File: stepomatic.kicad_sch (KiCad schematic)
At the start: 30 parts, among them J1 I2C, J2 Conn_01x05, J4 USB_B_Micro, Q1 MMBT3904, Q2 MMBT3904, SW1 Mode, SW2 RST, U1 HDC1080DMBR, U2 AMS1117-3.3, U3 ULN2003A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

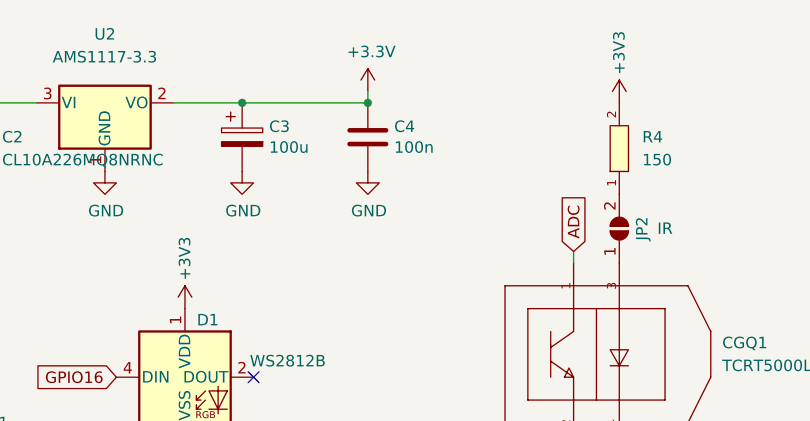
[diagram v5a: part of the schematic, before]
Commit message: Fix wrong capacitor
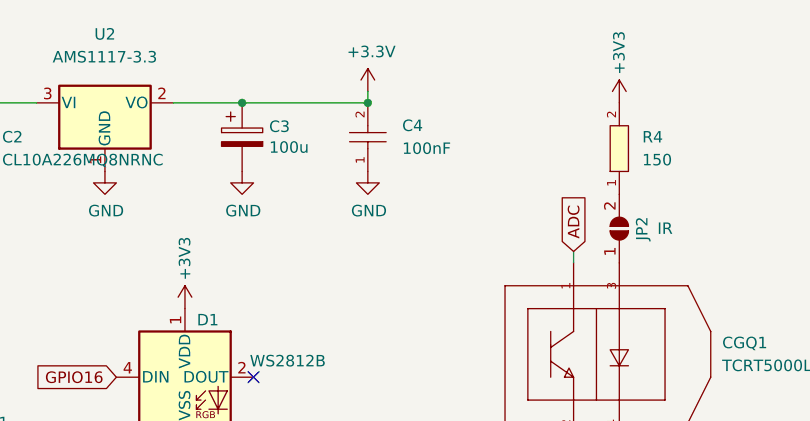
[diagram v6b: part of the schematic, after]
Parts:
- removed C4: 100n, Capacitor_SMD:C_0805_2012Metric, symbol Device:C
- added C4: 100nF, footprint:C0402, symbol CL05B104KO5NNNC:CL05B104KO5NNNC
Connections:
- net +3V3: now also C4.2
- net GND: now also C4.1
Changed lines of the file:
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@@
     (company "Besmer Labs")
   )
+  (junction (at 207.01 39.37) (diameter 0) (color 0 0 0 0)
+  )
   (junction (at 193.04 39.37) (diameter 0) (color 0 0 0 0)
-  )
-  (junction (at 207.01 39.37) (diameter 0) (color 0 0 0 0)
   )
   (junction (at 88.9 81.28) (diameter 0) (color 0 0 0 0)
@@
     (pin "4")
   )
+  (symbol (lib_id "CL05B104KO5NNNC:CL05B104KO5NNNC") (at 207.01 43.18 90) (unit 1)
+    (in_bom yes) (on_board yes) (fields_autoplaced)
+    (property "Reference" "C4" (id 0) (at 210.82 41.9099 90)
+      (effects (font (size 1.27 1.27)) (justify right))
+    )
+    (property "Value" "100nF" (id 1) (at 210.82 44.4499 90)
+      (effects (font (size 1.27 1.27)) (justify right))
+    )
+    (property "Footprint" "footprint:C0402" (id 2) (at 217.17 43.18 0)
+      (effects (font (size 1.27 1.27) italic) hide)
+    )
+    (property "Datasheet" "https://item.szlcsc.com/15869.html" (id 3) (at 206.883 45.466 0)
+      (effects (font (size 1.27 1.27)) (justify left) hide)
+    )
+    (property "LCSC" "C1525" (id 4) (at 207.01 43.18 0)
+      (effects (font (size 1.27 1.27)) hide)
+    )
+    (property "JLC" "" (id 5) (at 207.01 43.18 0)
+      (effects (font (size 1.27 1.27)) hide)
+    )
+    (pin "1")
+    (pin "2")
+  )
   (symbol (lib_id "Mechanical:MountingHole") (at 125.73 142.24 0) (unit 1)
     (in_bom no) (on_board yes) (fields_autoplaced)
@@
     )
     (pin "1")
-  )
-  (symbol (lib_id "Device:C") (at 207.01 43.18 0) (unit 1)
-    (in_bom yes) (on_board yes)
-    (property "Reference" "C4" (id 0) (at 209.931 42.0116 0)
-      (effects (font (size 1.27 1.27)) (justify left))
-    )
-    (property "Value" "100n" (id 1) (at 209.931 44.323 0)
-      (effects (font (size 1.27 1.27)) (justify left))
-    )
-    (property "Footprint" "Capacitor_SMD:C_0805_2012Metric" (id 2) (at 207.9752 46.99 0)
-      (effects (font (size 1.27 1.27)) hide)
-    )
-    (property "Datasheet" "~" (id 3) (at 207.01 43.18 0)
-      (effects (font (size 1.27 1.27)) hide)
-    )
-    (property "JLC" "" (id 5) (at 207.01 43.18 0)
-      (effects (font (size 1.27 1.27)) hide)
-    )
-    (property "LCSC" "C15008" (id 6) (at 209.931 42.0116 0)
-      (effects (font (size 1.27 1.27)) hide)
-    )
-    (pin "1")
-    (pin "2")
   )
   (symbol (lib_id "Mechanical:MountingHole") (at 125.095 161.29 0) (unit 1)
@@
       (reference "C3") (unit 1) (value "100u") (footprint "footprint:CASE-B_3528")
     )
-    (path "/997e98a3-7fb1-4b0a-aef3-53f70b9f03e9"
-      (reference "C4") (unit 1) (value "100n") (footprint "Capacitor_SMD:C_0805_2012Metric")
+    (path "/060122c0-b2a7-48a4-b1fe-01044e6f558d"
+      (reference "C4") (unit 1) (value "100nF") (footprint "footprint:C0402")
     )
     (path "/5bb5ca00-b4de-4288-b93f-8dde24e62e4c"

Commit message: Remove JLC property
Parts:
- J2: JLC_URL https://jlcpcb.com/partdetail/Jst-B5B_EH_LF_SN/C157991 -> (none)
- SW1, SW2: JLC_URL https://jlcpcb.com/partdetail/XkbConnectivity-TS_1187A_B_AB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 -> (none)
- U2: JLC_URL https://jlcpcb.com/partdetail/Advanced_MonolithicSystems-AM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 -> (none)
- U3: JLC_URL https://jlcpcb.com/partdetail/TexasInstruments-ULN2003ADR/C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 -> (none)
- U4: JLC_URL https://jlcpcb.com/partdetail/wch_jiangsu_Qin_heng-CH340C/C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 -> (none)
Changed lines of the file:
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@@
-      (effects (font (size 1.27 1.27)) hide)
-    )
-    (property "JLC" "" (id 5) (at 207.01 43.18 0)
       (effects (font (size 1.27 1.27)) hide)
     )
@@
       (effects (font (size 1.27 1.27)) hide)
     )
-    (property "JLC" "" (id 4) (at 125.73 142.24 0)
-      (effects (font (size 1.27 1.27)) hide)
-    )
     (property "LCSC" "DNP" (id 5) (at 125.73 142.24 0)
       (effects (font (size 1.27 1.27)) hide)
@@
       (effects (font (size 1.27 1.27)) hide)
     )
-    (property "JLC" "" (id 4) (at 125.73 154.94 0)
-      (effects (font (size 1.27 1.27)) hide)
-    )
     (property "LCSC" "DNP" (id 5) (at 125.73 154.94 0)
       (effects (font (size 1.27 1.27)) hide)
@@
     )
     (property "Datasheet" "~" (id 3) (at 193.04 43.18 0)
-      (effects (font (size 1.27 1.27)) hide)
-    )
-    (property "JLC" "" (id 5) (at 193.04 43.18 0)
       (effects (font (size 1.27 1.27)) hide)
     )
@@
       (effects (font (size 1.27 1.27)) (justify left top) hide)
     )
-    (property "JLC" "" (id 4) (at 186.69 69.85 0)
-      (effects (font (size 1.27 1.27)) hide)
-    )
     (property "LCSC" "DNP" (id 5) (at 186.69 69.85 0)
       (effects (font (size 1.27 1.27)) hide)
@@
       (effects (font (size 1.27 1.27)) (justify left) hide)
     )
-    (property "JLC" "" (id 5) (at 46.99 135.89 0)
-      (effects (font (size 1.27 1.27)) hide)
-    )
     (property "LCSC" "C20526" (id 6) (at 41.91 134.6199 0)
       (effects (font (size 1.27 1.27)) hide)
@@
     )
     (property "LCSC" "C1525" (id 4) (at 83.82 66.04 0)
-      (effects (font (size 1.27 1.27)) hide)
-    )
-    (property "JLC" "" (id 5) (at 83.82 66.04 0)
       (effects (font (size 1.27 1.27)) hide)
     )
@@
       (effects (font (size 1.27 1.27)) hide)
     )
-    (property "JLC" "" (id 4) (at 234.95 53.34 0)
-      (effects (font (size 1.27 1.27)) hide)
-    )
     (property "LCSC" "DNP" (id 5) (at 234.95 53.34 0)
       (effects (font (size 1.27 1.27)) hide)
@@
       (effects (font (size 1.27 1.27)) hide)
     )
-    (property "JLC" "" (id 5) (at 95.25 66.04 0)
-      (effects (font (size 1.27 1.27)) hide)
-    )
     (pin "1")
     (pin "2")
@@
     )
     (property "LCSC" "C22961" (id 4) (at 121.92 86.36 0)
-      (effects (font (size 1.27 1.27)) hide)
-    )
-    (property "JLC" "" (id 5) (at 121.92 86.36 0)
       (effects (font (size 1.27 1.27)) hide)
     )
@@
       (effects (font (size 1.27 1.27)) hide)
     )
-    (property "JLC_URL" "https://jlcpcb.com/partdetail/Advanced_MonolithicSystems-AMS1117_33/C6186" (id 5) (at 177.8 39.37 0)
-      (effects (font (size 1.27 1.27)) hide)
-    )
-    (property "JLC" "" (id 6) (at 177.8 39.37 0)
-      (effects (font (size 1.27 1.27)) hide)
-    )
     (property "LCSC" "C6186" (id 7) (at 177.8 31.75 0)
       (effects (font (size 1.27 1.27)) hide)
@@
       (effects (font (size 1.27 1.27)) hide)
     )
-    (property "JLC" "" (id 5) (at 55.88 149.86 0)
-      (effects (font (size 1.27 1.27)) hide)
-    )
     (property "LCSC" "C25752" (id 6) (at 55.88 146.05 0)
       (effects (font (size 1.27 1.27)) hide)
@@
     )
     (property "LCSC" "C59461" (id 4) (at 162.56 44.45 0)
-      (effects (font (size 1.27 1.27)) hide)
-    )
-    (property "JLC" "" (id 5) (at 162.56 44.45 0)
       (effects (font (size 1.27 1.27)) hide)
     )
@@
       (effects (font (size 1.27 1.27)) hide)
     )
-    (property "JLC" "" (id 4) (at 125.095 161.29 0)
-      (effects (font (size 1.27 1.27)) hide)
-    )
     (property "LCSC" "DNP" (id 5) (at 125.095 161.29 0)
       (effects (font (size 1.27 1.27)) hide)
@@
     )
     (property "Datasheet" "~" (id 3) (at 125.73 148.59 0)
-      (effects (font (size 1.27 1.27)) hide)
-    )
-    (property "JLC" "" (id 4) (at 125.73 148.59 0)
       (effects (font (size 1.27 1.27)) hide)
     )
@@
     )
     (property "Datasheet" "http://www.ti.com/lit/ds/symlink/uln2003a.pdf" (id 3) (at 204.47 125.73 0)
-      (effects (font (size 1.27 1.27)) hide)
-    )
-    (property "JLC_URL" "https://jlcpcb.com/partdetail/TexasInstruments-ULN2003ADR/C7512" (id 5) (at 201.93 120.65 0)
-      (effects (font (size 1.27 1.27)) hide)
-    )
-    (property "JLC" "" (id 6) (at 201.93 120.65 0)
       (effects (font (size 1.27 1.27)) hide)
     )
@@
       (effects (font (size 1.27 1.27)) hide)
     )
-    (property "JLC" "" (id 5) (at 55.88 135.89 0)
-      (effects (font (size 1.27 1.27)) hide)
-    )
     (property "LCSC" "C25752" (id 6) (at 55.88 130.81 0)
       (effects (font (size 1.27 1.27)) hide)
@@
     )
     (property "Datasheet" "https://docs.ai-thinker.com/_media/esp8266/docs/esp-07s_product_specification_en.pdf" (id 3) (at 135.89 95.25 0)
-      (effects (font (size 1.27 1.27)) hide)
-    )
-    (property "JLC" "" (id 5) (at 144.78 97.79 0)
       (effects (font (size 1.27 1.27)) hide)
     )
@@
       (effects (font (size 1.27 1.27)) (justify left) hide)
     )
-    (property "JLC" "" (id 5) (at 46.99 149.86 0)
-      (effects (font (size 1.27 1.27)) hide)
-    )
     (property "LCSC" "C20526" (id 6) (at 41.91 148.5899 0)
       (effects (font (size 1.27 1.27)) hide)
@@
     )
     (property "Datasheet" "~" (id 3) (at 165.1 77.47 0)
-      (effects (font (size 1.27 1.27)) hide)
-    )
-    (property "JLC" "" (id 4) (at 165.1 82.55 0)
-      (effects (font (size 1.27 1.27)) hide)
-    )
-    (property "JLC_URL" "https://jlcpcb.com/partdetail/XkbConnectivity-TS_1187A_B_AB/C318884" (id 5) (at 165.1 82.55 0)
       (effects (font (size 1.27 1.27)) hide)
     )
@@
       (effects (font (size 1.27 1.27)) hide)
     )
-    (property "JLC" "" (id 4) (at 163.83 107.95 0)
-      (effects (font (size 1.27 1.27)) hide)
-    )
     (property "LCSC" "DNP" (id 5) (at 163.83 107.95 0)
       (effects (font (size 1.27 1.27)) hide)
@@
     )
     (property "Datasheet" "~" (id 3) (at 66.04 95.25 0)
-      (effects (font (size 1.27 1.27)) hide)
-    )
-    (property "JLC" "" (id 4) (at 62.23 93.98 0)
       (effects (font (size 1.27 1.27)) hide)
     )
@@
       (effects (font (size 1.27 1.27)) hide)
     )
-    (property "JLC" "" (id 4) (at 224.79 128.27 0)
-      (effects (font (size 1.27 1.27)) hide)
-    )
-    (property "JLC_URL" "https://jlcpcb.com/partdetail/Jst-B5B_EH_LF_SN/C157991" (id 5) (at 224.79 128.27 0)
-      (effects (font (size 1.27 1.27)) hide)
-    )
     (property "LCSC" "C157991" (id 6) (at 227.584 129.5401 0)
       (effects (font (size 1.27 1.27)) hide)
@@
     )
     (property "Datasheet" "https://datasheet.lcsc.com/szlcsc/Jiangsu-Qin-Heng-CH340C_C84681.pdf" (id 3) (at 80.01 76.2 0)
-      (effects (font (size 1.27 1.27)) hide)
-    )
-    (property "JLC_URL" "https://jlcpcb.com/partdetail/wch_jiangsu_Qin_heng-CH340C/C7464026" (id 5) (at 88.9 96.52 0)
-      (effects (font (size 1.27 1.27)) hide)
-    )
-    (property "JLC" "" (id 6) (at 88.9 96.52 0)
       (effects (font (size 1.27 1.27)) hide)
     )
@@
       (effects (font (size 1.27 1.27)) hide)
     )
-    (property "JLC" "" (id 5) (at 232.41 67.31 0)
-      (effects (font (size 1.27 1.27)) hide)
-    )
     (pin "1")
     (pin "2")
@@
       (effects (font (size 1.27 1.27)) hide)
     )
-    (property "JLC" "" (id 4) (at 127 64.77 0)
-      (effects (font (size 1.27 1.27)) hide)
-    )
-    (property "JLC_URL" "https://jlcpcb.com/partdetail/XkbConnectivity-TS_1187A_B_AB/C318884" (id 5) (at 127 64.77 0)
-      (effects (font (size 1.27 1.27)) hide)
-    )

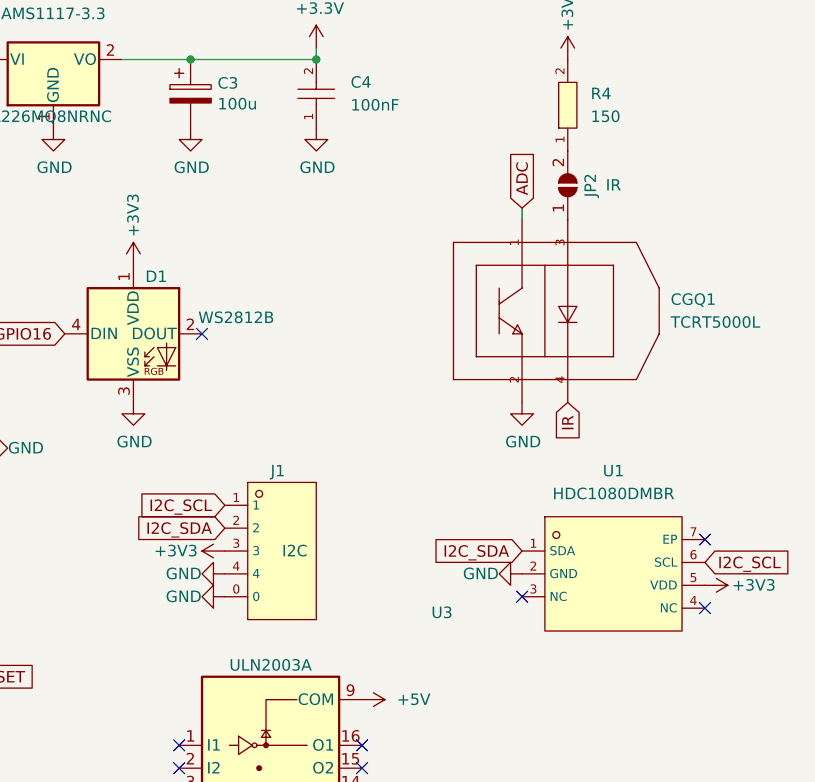
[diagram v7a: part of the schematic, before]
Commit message: Fix rotation of I2C connector
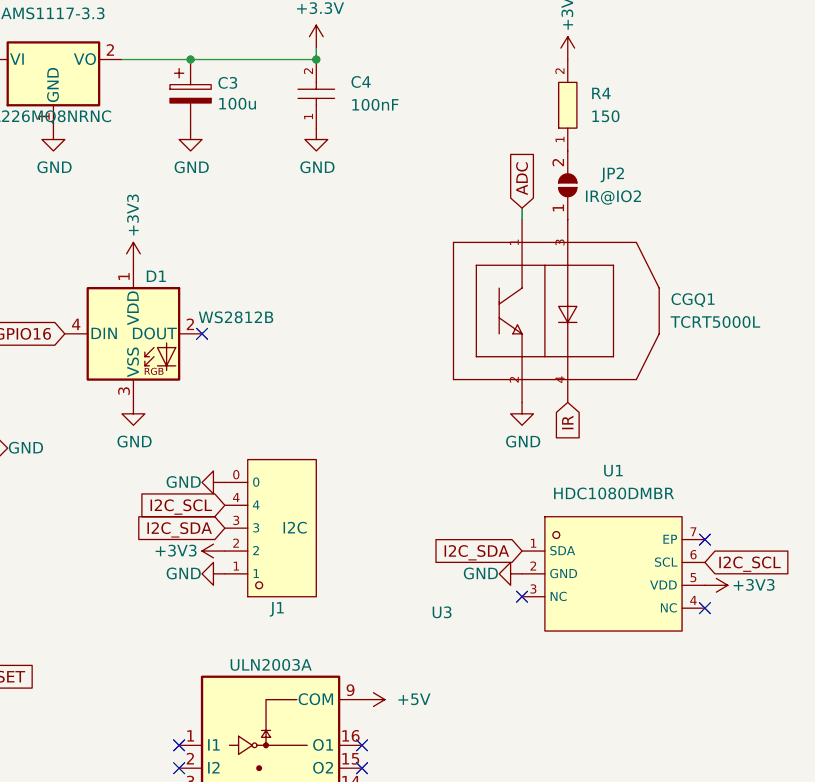
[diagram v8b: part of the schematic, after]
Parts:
- JP2: value IR -> IR@IO2
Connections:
- net +3V3: now also J1.2; no longer J1.3
- net GND: now also J1.1; no longer J1.4
- net I2C_SCL: now also J1.4; no longer J1.1
- net I2C_SDA: now also J1.3; no longer J1.2
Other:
- moved on the sheet: J1
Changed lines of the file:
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@@
     (pin "2")
   )
-  (symbol (lib_id "BM04B-SRSS-TB(LF)(SN):BM04B-SRSS-TB(LF)(SN)") (at 201.93 93.98 0) (unit 1)
-    (in_bom yes) (on_board yes)
-    (property "Reference" "J1" (id 0) (at 201.93 85.09 0)
-      (effects (font (size 1.27 1.27)) (justify left))
-    )
-    (property "Value" "I2C" (id 1) (at 203.2 93.98 0)
-      (effects (font (size 1.27 1.27)) (justify left))
-    )
-    (property "Footprint" "footprint:CONN-SMD_BM04B-SRSS-TB" (id 2) (at 201.93 104.14 0)
+  (symbol (lib_id "BM04B-SRSS-TB(LF)(SN):BM04B-SRSS-TB(LF)(SN)") (at 201.93 91.44 0) (mirror x) (unit 1)
+    (in_bom yes) (on_board yes)
+    (property "Reference" "J1" (id 0) (at 201.93 100.33 0)
+      (effects (font (size 1.27 1.27)) (justify left))
+    )
+    (property "Value" "I2C" (id 1) (at 203.2 91.44 0)
+      (effects (font (size 1.27 1.27)) (justify left))
+    )
+    (property "Footprint" "footprint:CONN-SMD_BM04B-SRSS-TB" (id 2) (at 201.93 81.28 0)
       (effects (font (size 1.27 1.27) italic) hide)
     )
-    (property "Datasheet" "https://item.szlcsc.com/171770.html" (id 3) (at 199.644 93.853 0)
+    (property "Datasheet" "https://item.szlcsc.com/171770.html" (id 3) (at 199.644 91.567 0)
       (effects (font (size 1.27 1.27)) (justify left) hide)
     )
-    (property "LCSC" "C160390" (id 4) (at 201.93 93.98 0)
+    (property "LCSC" "C160390" (id 4) (at 201.93 91.44 0)
       (effects (font (size 1.27 1.27)) hide)
     )
@@
     (pin "1")
   )
-  (symbol (lib_id "power:GND") (at 196.85 99.06 270) (unit 1)
-    (in_bom yes) (on_board yes)
-    (property "Reference" "#PWR0121" (id 0) (at 190.5 99.06 0)
-      (effects (font (size 1.27 1.27)) hide)
-    )
-    (property "Value" "GND" (id 1) (at 192.278 99.06 90))
-    (property "Footprint" "" (id 2) (at 196.85 99.06 0)
-      (effects (font (size 1.27 1.27)) hide)
-    )
-    (property "Datasheet" "" (id 3) (at 196.85 99.06 0)
+  (symbol (lib_id "power:GND") (at 196.85 86.36 270) (mirror x) (unit 1)
+    (in_bom yes) (on_board yes)
+    (property "Reference" "#PWR0121" (id 0) (at 190.5 86.36 0)
+      (effects (font (size 1.27 1.27)) hide)
+    )
+    (property "Value" "GND" (id 1) (at 192.278 86.36 90))
+    (property "Footprint" "" (id 2) (at 196.85 86.36 0)
+      (effects (font (size 1.27 1.27)) hide)
+    )
+    (property "Datasheet" "" (id 3) (at 196.85 86.36 0)
       (effects (font (size 1.27 1.27)) hide)
     )
@@
   (symbol (lib_id "Jumper:SolderJumper_2_Open") (at 234.95 53.34 90) (unit 1)
     (in_bom no) (on_board yes)
-    (property "Reference" "JP2" (id 0) (at 237.49 53.34 0))
-    (property "Value" "IR" (id 1) (at 240.03 53.34 90))
+    (property "Reference" "JP2" (id 0) (at 240.03 52.07 90))
+    (property "Value" "IR@IO2" (id 1) (at 240.03 54.61 90))
     (property "Footprint" "Jumper:SolderJumper-2_P1.3mm_Open_TrianglePad1.0x1.5mm" (id 2) (at 234.95 53.34 0)
       (effects (font (size 1.27 1.27)) hide)
@@
     )
     (path "/43e716f9-4dd6-4610-ae07-63de1d43abf8"
-      (reference "JP2") (unit 1) (value "IR") (footprint "Jumper:SolderJumper-2_P1.3mm_Open_TrianglePad1.0x1.5mm")
+      (reference "JP2") (unit 1) (value "IR@IO2") (footprint "Jumper:SolderJumper-2_P1.3mm_Open_TrianglePad1.0x1.5mm")
     )
     (path "/3848a93b-ec2e-4c69-980c-bcbbecd16bc8"
